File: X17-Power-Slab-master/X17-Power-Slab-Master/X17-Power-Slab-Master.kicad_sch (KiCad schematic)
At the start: 15 parts, among them J1 Conn_01x12_Pin, J2 ET60T-D04-3-08-D04-X-R1-S, J3 796636-6, Q2 TSM340N06CP ROG

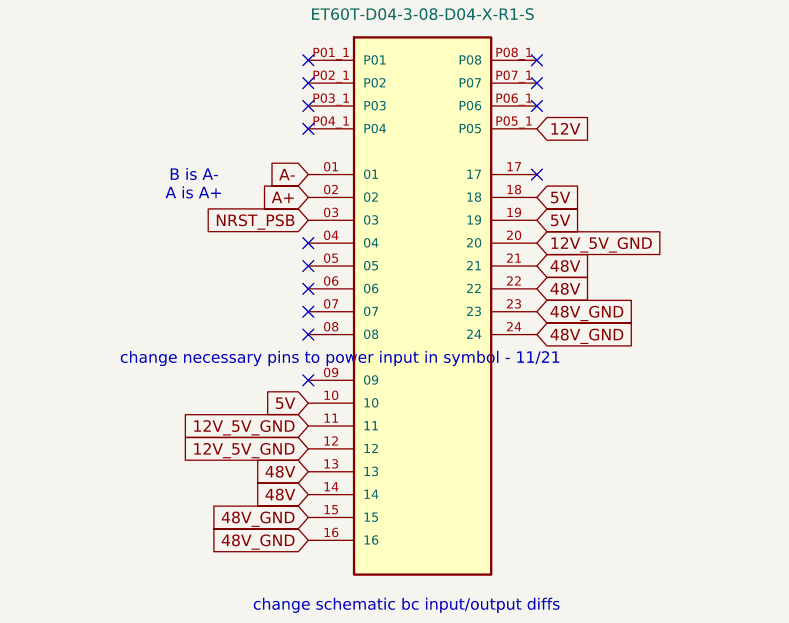
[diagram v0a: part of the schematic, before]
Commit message: some pinout changes
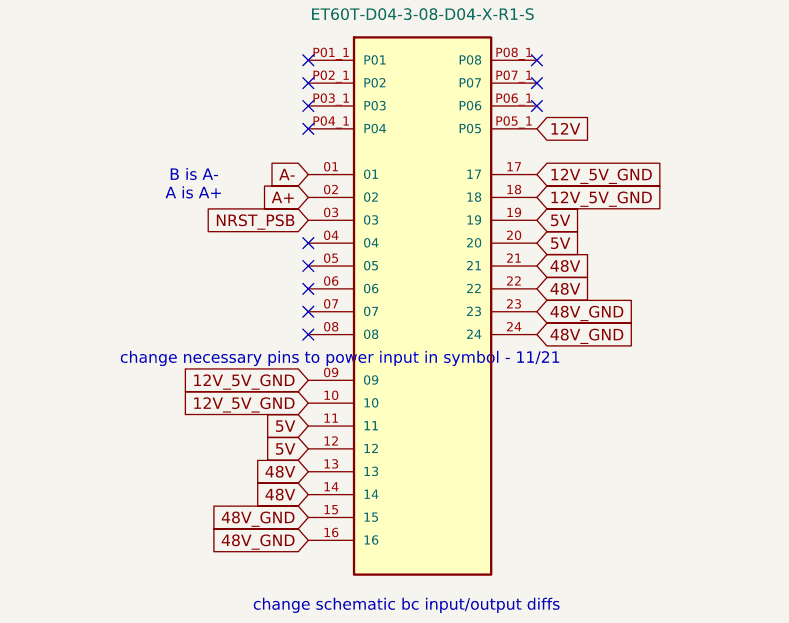
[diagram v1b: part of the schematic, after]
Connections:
- net 12V_5V_GND: now also J2.09, J2.10, J2.17, J2.18; no longer J2.11, J2.12, J2.20
- net 5V: now also J2.11, J2.12, J2.20; no longer J2.10, J2.18
- no-connect marks 16 -> 14
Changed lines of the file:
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@@
-	)
-	(no_connect
-		(at 240.03 73.66)
 	)
 	(no_connect
@@
 	(no_connect
 		(at 240.03 58.42)
-	)
-	(no_connect
-		(at 265.43 50.8)
 	)
 	(no_connect
@@
 	(global_label "12V_5V_GND"
 		(shape input)
-		(at 240.03 78.74 180)
-		(fields_autoplaced yes)
-		(effects
-			(font
-				(size 1.27 1.27)
-			)
-			(justify right)
-		)
-		(property "Intersheetrefs" "${INTERSHEET_REFS}"
-			(at 225.4334 78.74 0)
+		(at 240.03 73.66 180)
+		(fields_autoplaced yes)
+		(effects
+			(font
+				(size 1.27 1.27)
+			)
+			(justify right)
+		)
+		(property "Intersheetrefs" "${INTERSHEET_REFS}"
+			(at 225.4334 73.66 0)
 			(effects
 				(font
@@
 		)
 	)
+	(global_label "5V"
+		(shape input)
+		(at 240.03 81.28 180)
+		(fields_autoplaced yes)
+		(effects
+			(font
+				(size 1.27 1.27)
+			)
+			(justify right)
+		)
+		(property "Intersheetrefs" "${INTERSHEET_REFS}"
+			(at 234.7467 81.28 0)
+			(effects
+				(font
+					(size 1.27 1.27)
+				)
+				(justify right)
+				(hide yes)
+			)
+		)
+	)
 	(global_label "48V_GND"
 		(shape input)
@@
 	(global_label "5V"
 		(shape input)
-		(at 265.43 53.34 0)
+		(at 265.43 58.42 0)
 		(fields_autoplaced yes)
 		(effects
@@
 		)
 		(property "Intersheetrefs" "${INTERSHEET_REFS}"
-			(at 270.7133 53.34 0)
+			(at 270.7133 58.42 0)
 			(effects
 				(font
@@
 	(global_label "12V_5V_GND"
 		(shape input)
-		(at 265.43 58.42 0)
+		(at 265.43 50.8 0)
 		(fields_autoplaced yes)
 		(effects
@@
 		)
 		(property "Intersheetrefs" "${INTERSHEET_REFS}"
-			(at 280.0266 58.42 0)
+			(at 280.0266 50.8 0)
 			(effects
 				(font
@@
 	(global_label "12V_5V_GND"
 		(shape input)
-		(at 240.03 81.28 180)
-		(fields_autoplaced yes)
-		(effects
-			(font
-				(size 1.27 1.27)
-			)
-			(justify right)
-		)
-		(property "Intersheetrefs" "${INTERSHEET_REFS}"
-			(at 225.4334 81.28 0)
-			(effects
-				(font
-					(size 1.27 1.27)
-				)
-				(justify right)
+		(at 240.03 76.2 180)
+		(fields_autoplaced yes)
+		(effects
+			(font
+				(size 1.27 1.27)
+			)
+			(justify right)
+		)
+		(property "Intersheetrefs" "${INTERSHEET_REFS}"
+			(at 225.4334 76.2 0)
+			(effects
+				(font
+					(size 1.27 1.27)
+				)
+				(justify right)
+				(hide yes)
+			)
+		)
+	)
+	(global_label "12V_5V_GND"
+		(shape input)
+		(at 265.43 53.34 0)
+		(fields_autoplaced yes)
+		(effects
+			(font
+				(size 1.27 1.27)
+			)
+			(justify left)
+		)
+		(property "Intersheetrefs" "${INTERSHEET_REFS}"
+			(at 280.0266 53.34 0)
+			(effects
+				(font
+					(size 1.27 1.27)
+				)
+				(justify left)
 				(hide yes)
 			)
@@
 	(global_label "5V"
 		(shape input)
-		(at 240.03 76.2 180)
-		(fields_autoplaced yes)
-		(effects
-			(font
-				(size 1.27 1.27)
-			)
-			(justify right)
-		)
-		(property "Intersheetrefs" "${INTERSHEET_REFS}"
-			(at 234.7467 76.2 0)
-			(effects
-				(font
+		(at 240.03 78.74 180)
+		(fields_autoplaced yes)
+		(effects
+			(font
+				(size 1.27 1.27)
+			)
+			(justify right)
+		)
+		(property "Intersheetrefs" "${INTERSHEET_REFS}"
+			(at 234.7467 78.74 0)
+			(effects
+				(font
